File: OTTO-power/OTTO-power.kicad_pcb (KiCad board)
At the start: 2 copper layers, 72.5 x 23.5 mm, 48 parts, among them J201 Barrel_Jack, J202 Conn_01x10, J203 USB_B_Micro, J204 battery, SW201 SW_Push, SW202 SW_reset, U201 TPS61090, U202 MAX8903A, U203 XC6210, U204 MAX17048

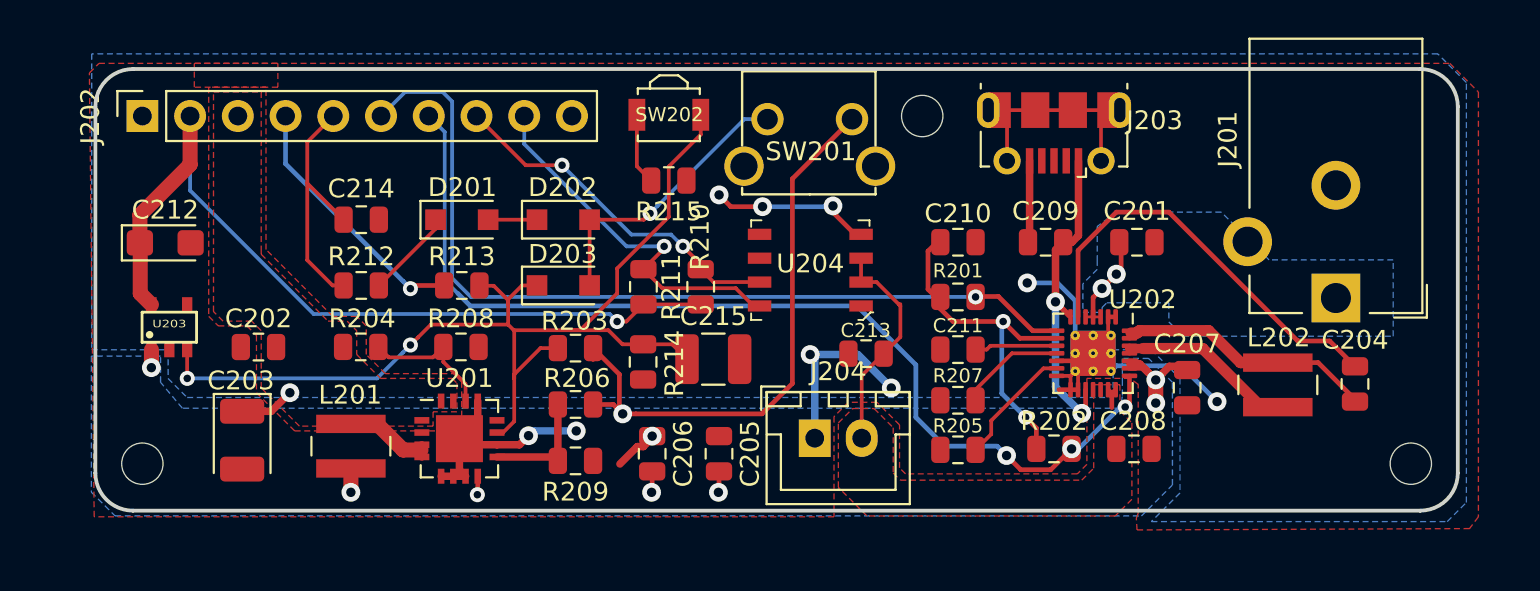
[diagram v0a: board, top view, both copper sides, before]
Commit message: Add files via upload
Attempted to consolidate some of the traces and component placement for the OTTO power board. Only current outstanding item is double checking via sizing for max current load and overall QA check of board. Committing changes to dev branch instead of incorrectly to the master branch (like the first upload).
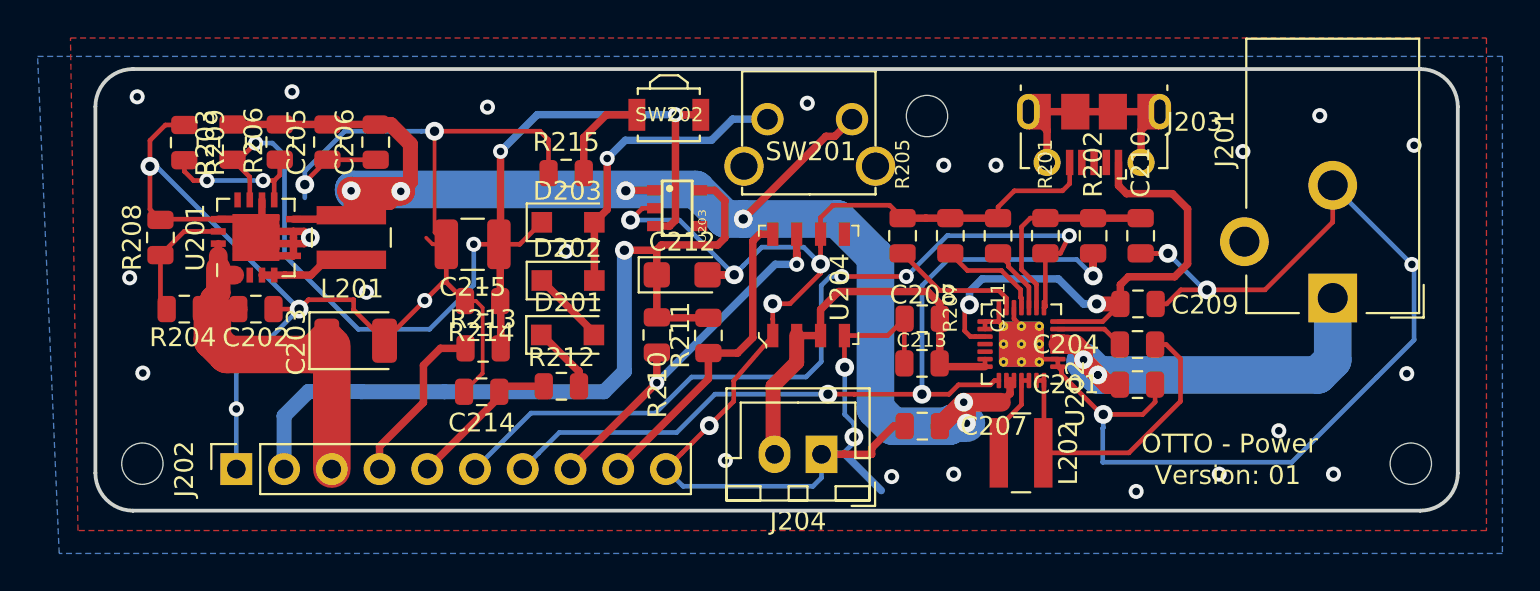
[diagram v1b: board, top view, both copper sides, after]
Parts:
- moved U203 27.8 mm to (180.4, 31.2), turned to 270 degrees
- moved C212 27.6 mm to (180.7, 34.8)
- moved R209 26.8 mm to (154.2, 27.7), turned to 270 degrees
- moved C205 26.6 mm to (161.8, 27.7), turned to 90 degrees
- moved C206 22.2 mm to (164.4, 27.7), turned to 90 degrees
- moved R203 21.3 mm to (156.8, 27.7), turned to 90 degrees
- moved R206 21.0 mm to (159.3, 27.7), turned to 90 degrees
- moved J202 19.4 mm to (157.0, 45.1)
- moved R208 17.0 mm to (152.9, 32.8), turned to 270 degrees
- moved U201 15.2 mm to (158.0, 32.8), turned to 90 degrees
- moved C207 14.2 mm to (193.5, 42.8), turned to 0 degrees
- moved C215 14.2 mm to (169.6, 33.1), turned to 180 degrees
- moved L202 14.1 mm to (198.7, 44.2), turned to 0 degrees
- moved C208 13.2 mm to (193.5, 37.1), turned to 0 degrees
- moved R212 11.9 mm to (174.3, 40.7)
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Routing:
- net GNDA: track 58.7 -> 242.9 mm, vias 10 -> 39
- net SYS: track 44.7 -> 85.6 mm, vias 8 -> 6
- net Net-(C204-Pad1): track 22.5 -> 3.64 mm
- net 5V: track 2.95 -> 21.6 mm, vias 1 -> 0
- net DC: track 5.39 -> 22.4 mm, vias 2 -> 3
- net USB: track 17.3 -> 29.4 mm
- net BATT+: track 13.5 -> 22.9 mm
- net CHG_OUT: track 54.3 -> 45.5 mm
- net VL: track 18.8 -> 11.2 mm, vias 2 -> 0
- net SENSE_PIN: track 13.5 -> 8.19 mm
- net Net-(L202-Pad1): track 9.84 -> 4.75 mm
- net OUT_PIN: track 13.8 -> 9.10 mm, vias 1 -> 0
- net DOK_OUT: track 47.3 -> 44.0 mm, vias 1 -> 3
- net SDA: track 19.9 -> 17.2 mm, vias 1 -> 0
- net Net-(C204-Pad2): track 14.2 -> 16.6 mm
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- removed copper zone on F.Cu, net 5V
- removed copper zone on F.Cu, net BATT+
- removed copper zone on B.Cu, net DC
- removed copper zone on B.Cu, net SYS
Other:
- board text added: "OTTO - Power"
- board text added: "Version: 01"
